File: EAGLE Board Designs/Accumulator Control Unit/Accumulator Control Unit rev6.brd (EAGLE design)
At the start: 255 x 73 mm, 302 parts, among them J1 CONNECTOR-12_MF_T_V_, J2 CONNECTOR-6_μF_T_V_BLACK, J3 CONNECTOR-4_μF_T_V_BLACK, J4 CONNECTOR-2_MF_T_V_, J5 CONNECTOR-8_μF_T_V_BLACK, J6 CONNECTOR-16_MF_T_V_, J9 CONNECTOR-2_MF_T_V_, Q1 TRANSISTOR_N_MOS__PMV15ENEA, Q2 TRANSISTOR_N_MOS__PMV15ENEA, Q3 TRANSISTOR_N_MOS__PMV15ENEA, Q4 TRANSISTOR_N_MOS__PMV15ENEA, Q5 TRANSISTOR_P_MOS_SOT-23_DMP30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, T1 TRANSFORMER_HM2112ZNLT_AIRGAP, U1 VOLTAGE_REGULATOR_SOT-223_3.3V, U10 TCAN1051HQV-Q1, U11 OPAMP_1_CHANNEL_OPA991, U12 OPAMP_1_CHANNEL_OPA991, U13 OPAMP_1_CHANNEL_OPA991, U14 RELAY_SOLIDSTATE_NO_DIP-4, U15 LM555, U16 OPAMP_1_CHANNEL_OPA991, U17 OPAMP_2_CHANNEL_OPA_2991, U18 OPAMP_1_CHANNEL_OPA991, U19 OPAMP_2_CHANNEL_OPA_2991, U2 RELAY_SOLIDSTATE_NO_DIP-4, U20 LOGICGATE_BUFFER, U21 ADM8316WBX30, U22 OPAMP_1_CHANNEL_OPA991, U23 LOGICGATE_AND_DCK3, U24 LOGICGATE_AND_DCK3, U25 LOGICGATE_AND_DCK3, U26 OPAMP_1_CHANNEL_OPA991, U27 ADG1423, U28 OPAMP_1_CHANNEL_OPA991, U29 OPAMP_2_CHANNEL_OPA_2991, U3 RELAY_SOLIDSTATE_NO_DIP-4, U30 OPAMP_1_CHANNEL_OPA991, U31 OPAMP_2_CHANNEL_OPA_2991, U32 LTC6820, U33 OPAMP_1_CHANNEL_OPA991, U4 OPAMP_1_CHANNEL_OPA991, U5 OPAMP_1_CHANNEL_OPA991, U6 TCAN1051HQV-Q1, U7 LTC6820, U8 OPAMP_1_CHANNEL_OPA991, U9 OPAMP_1_CHANNEL_OPA991

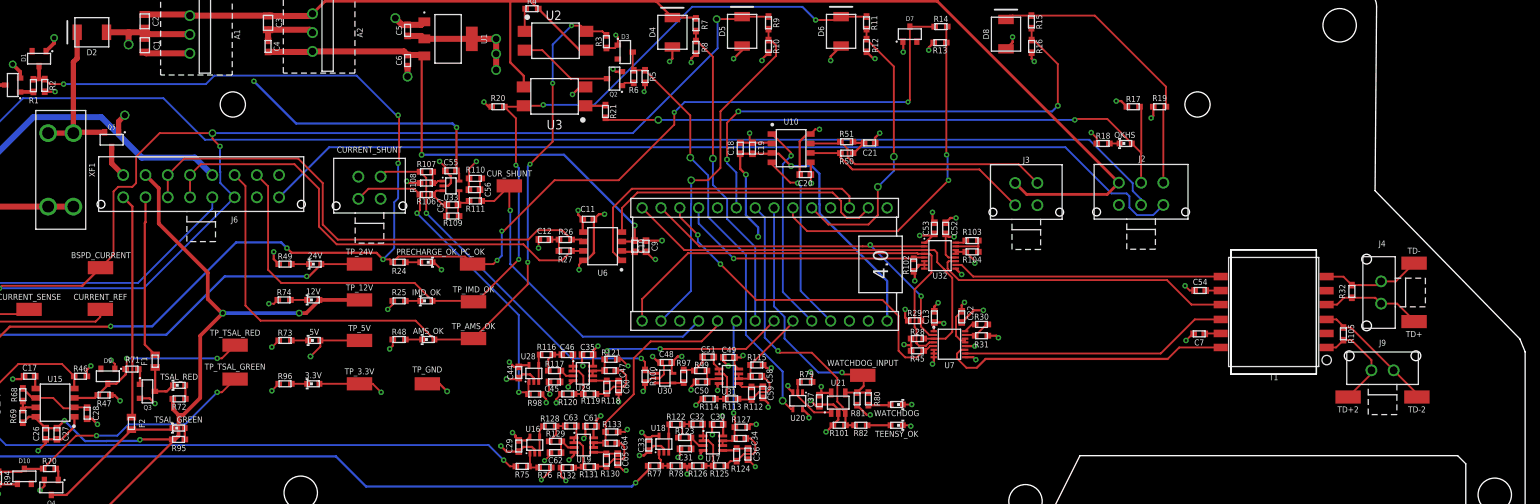
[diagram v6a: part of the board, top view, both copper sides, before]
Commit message: Added HV silkscreen
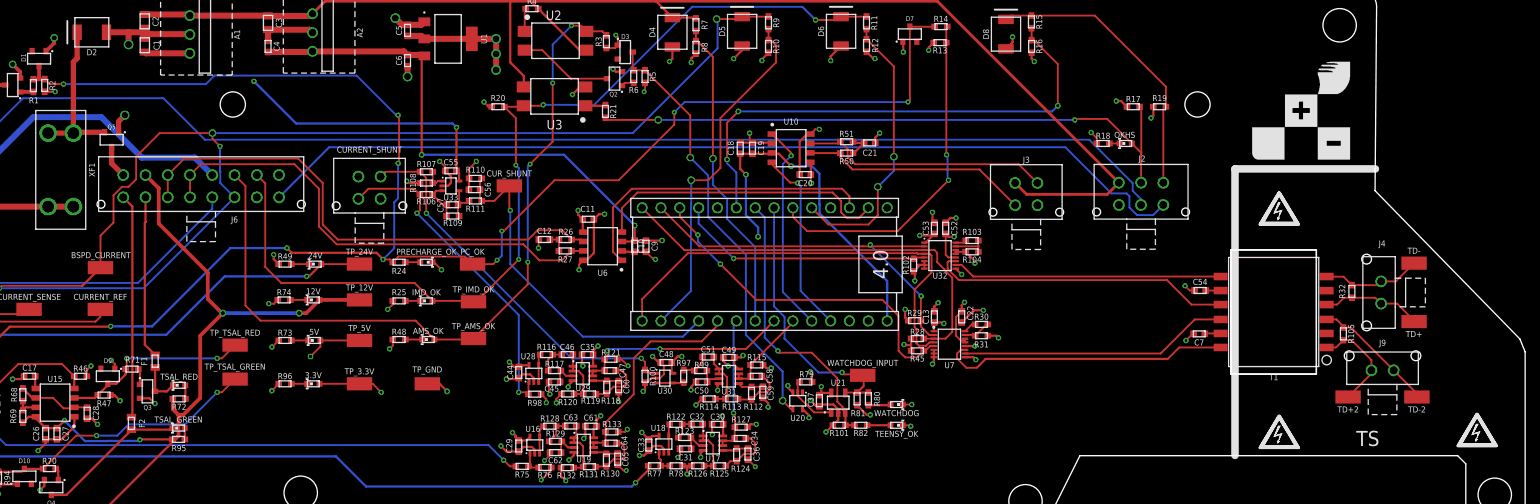
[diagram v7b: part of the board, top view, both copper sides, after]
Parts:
- added U$10, U$11, U$13, U$14, U$15, U$16: (no value), HyTechManufacturing:HV_MEDIUM
- added U$12: (no value), HyTechManufacturing:LOGO_HYTECH_SQUARE_EXTRA_LARGE
- added U$9: (no value), HyTechManufacturing:TS
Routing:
- net PRECHARGE_OK: track 263.4 -> 262.7 mm
- net BSPD_CURRENT: track 179.6 -> 179.0 mm
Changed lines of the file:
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@@
 <wire x1="249.428" y1="0" x2="252.5" y2="0" width="0" layer="20"/>
 <wire x1="252.5" y1="0" x2="255" y2="2.5" width="0" layer="20"/>
+<wire x1="215.9" y1="10.033" x2="215.9" y2="48.641" width="1.016" layer="21"/>
+<wire x1="215.9" y1="48.641" x2="234.823" y2="48.641" width="1.016" layer="21"/>
+<wire x1="234.823" y1="48.387" x2="234.569" y2="48.641" width="1.016" layer="22"/>
+<wire x1="234.569" y1="48.641" x2="215.9" y2="48.641" width="1.016" layer="22"/>
+<wire x1="215.9" y1="48.641" x2="215.773" y2="10.287" width="1.016" layer="22"/>
+<wire x1="215.773" y1="10.287" x2="215.9" y2="10.16" width="1.016" layer="22"/>
 </plain>
 <attributes>
@@
 <attribute name="NAME" x="64.516" y="54.61" size="0.635" layer="25" font="vector" align="top-center"/>
 </element>
+<element name="U$10" library="HyTechManufacturing" package="HV_MEDIUM" value="" x="221.869" y="13.208" smashed="yes"/>
+<element name="U$11" library="HyTechManufacturing" package="HV_MEDIUM" value="" x="248.539" y="13.462" smashed="yes"/>
+<element name="U$12" library="HyTechManufacturing" package="LOGO_HYTECH_SQUARE_EXTRA_LARGE" value="" x="224.79" y="56.515" smashed="yes"/>
+<element name="U$9" library="HyTechManufacturing" package="TS" value="" x="233.807" y="12.319" smashed="yes"/>
+<element name="U$13" library="HyTechManufacturing" package="HV_MEDIUM" value="" x="221.869" y="43.307" smashed="yes"/>
+<element name="U$14" library="HyTechManufacturing" package="HV_MEDIUM" value="" x="248.539" y="13.462" smashed="yes"/>
+<element name="U$15" library="HyTechManufacturing" package="HV_MEDIUM" value="" x="221.869" y="13.208" smashed="yes"/>
+<element name="U$16" library="HyTechManufacturing" package="HV_MEDIUM" value="" x="221.869" y="43.307" smashed="yes"/>
 </elements>
 <signals>
@@
 <via x="204.597" y="55.499" extent="1-16" drill="0.35"/>
 <wire x1="87.034" y1="35.814" x2="86.36" y2="36.488" width="0.3048" layer="1"/>
-<wire x1="86.36" y1="36.488" x2="86.36" y2="37.465" width="0.3048" layer="1"/>
-<via x="86.36" y="37.465" extent="1-16" drill="0.35"/>
+<wire x1="86.36" y1="36.488" x2="86.36" y2="37.084" width="0.3048" layer="1"/>
+<via x="86.36" y="37.084" extent="1-16" drill="0.35"/>
 <wire x1="133.2865" y1="61.7474" x2="132.4356" y2="61.7474" width="0.3048" layer="1"/>
 <wire x1="132.4356" y1="61.7474" x2="132.08" y2="62.103" width="0.3048" layer="1"/>
@@
 <wire x1="42.164" y1="8.1414" x2="43.7909" y2="8.1414" width="0.3048" layer="1"/>
 <wire x1="43.7909" y1="8.1414" x2="43.815" y2="8.1655" width="0.3048" layer="1"/>
-<wire x1="55.626" y1="13.9065" x2="55.626" y2="13.704" width="0.3048" layer="1"/>
 <wire x1="57.15" y1="13.704" x2="55.626" y2="13.704" width="0.3048" layer="1"/>
 <wire x1="110.986" y1="48.387" x2="111.336" y2="48.037" width="0.3048" layer="1"/>
@@
 <wire x1="52.5526" y1="14.4408" x2="53.3518" y2="15.24" width="0.3048" layer="1"/>
 <wire x1="53.3518" y1="15.24" x2="54.2925" y2="15.24" width="0.3048" layer="1"/>
-<wire x1="55.626" y1="13.704" x2="54.2925" y2="15.0375" width="0.3048" layer="1"/>
 <wire x1="54.2925" y1="15.0375" x2="54.2925" y2="15.24" width="0.3048" layer="1"/>
+<wire x1="55.626" y1="13.704" x2="54.2925" y2="15.0375" width="0.3048" layer="1"/>
 </signal>
 <signal name="BSPD_CURRENT">
@@
 <wire x1="78.105" y1="52.705" x2="78.105" y2="53.467" width="0.254" layer="1"/>
 <wire x1="67.818" y1="50.292" x2="70.993" y2="53.467" width="0.254" layer="1"/>
-<wire x1="64.77" y1="37.084" x2="64.77" y2="45.593" width="0.254" layer="1"/>
-<wire x1="64.77" y1="45.593" x2="65.405" y2="46.228" width="0.254" layer="1"/>
-<wire x1="65.405" y1="46.228" x2="67.31" y2="46.228" width="0.254" layer="1"/>
-<wire x1="67.31" y1="46.228" x2="67.818" y2="46.736" width="0.254" layer="1"/>
-<wire x1="63.0174" y1="35.3314" x2="64.77" y2="37.084" width="0.254" layer="1"/>
-<wire x1="67.818" y1="46.736" x2="67.818" y2="50.292" width="0.254" layer="1"/>
+<wire x1="64.77" y1="41.402" x2="64.77" y2="45.085" width="0.254" layer="1"/>
+<wire x1="64.77" y1="45.085" x2="65.913" y2="46.228" width="0.254" layer="1"/>
+<wire x1="65.913" y1="46.228" x2="66.802" y2="46.228" width="0.254" layer="1"/>
+<wire x1="66.802" y1="46.228" x2="67.818" y2="47.244" width="0.254" layer="1"/>
+<wire x1="64.77" y1="41.402" x2="63.0174" y2="39.6494" width="0.254" layer="1"/>
+<wire x1="63.0174" y1="35.3314" x2="63.0174" y2="39.6494" width="0.254" layer="1"/>
+<wire x1="67.818" y1="47.244" x2="67.818" y2="50.292" width="0.254" layer="1"/>
 </signal>
 <signal name="IMD_OK">
@@
 <contactref element="R11" pad="1"/>
 <contactref element="D6" pad="2"/>
-<wire x1="84.083" y1="47.817" x2="85.598" y2="46.302" width="0.254" layer="1"/>
+<wire x1="84.083" y1="47.817" x2="85.217" y2="46.683" width="0.254" layer="1"/>
 <wire x1="105.346" y1="33.274" x2="107.759" y2="30.861" width="0.254" layer="1"/>
-<wire x1="85.598" y1="46.302" x2="85.598" y2="35.052" width="0.254" layer="1"/>
-<wire x1="85.598" y1="35.052" x2="87.376" y2="33.274" width="0.254" layer="1"/>
+<wire x1="85.217" y1="46.683" x2="85.217" y2="35.433" width="0.254" layer="1"/>
+<wire x1="85.217" y1="35.433" x2="87.376" y2="33.274" width="0.254" layer="1"/>
 <wire x1="87.376" y1="33.274" x2="105.346" y2="33.274" width="0.254" layer="1"/>
 <wire x1="162.814" y1="69.163" x2="163.068" y2="69.163" width="0.254" layer="1"/>
@@
 <wire x1="64.3382" y1="27.3812" x2="50.7902" y2="27.3812" width="0.3048" layer="1"/>
 <wire x1="64.389" y1="27.432" x2="69.977" y2="27.432" width="0.3048" layer="16"/>
-<wire x1="69.977" y1="27.432" x2="81.28" y2="38.735" width="0.3048" layer="16"/>
-<wire x1="81.28" y1="38.735" x2="87.376" y2="38.735" width="0.3048" layer="16"/>
-<wire x1="87.376" y1="38.735" x2="88.138" y2="37.973" width="0.3048" layer="16"/>
+<wire x1="69.977" y1="27.432" x2="80.518" y2="37.973" width="0.3048" layer="16"/>
+<wire x1="80.518" y1="37.973" x2="88.138" y2="37.973" width="0.3048" layer="16"/>
 <via x="88.138" y="37.973" extent="1-16" drill="0.35"/>
 <wire x1="100.203" y1="37.338" x2="88.773" y2="37.338" width="0.3048" layer="1"/>
@@
 <wire x1="142.621" y1="47.117" x2="144.907" y2="47.117" width="0.254" layer="1"/>
 <wire x1="146.558" y1="48.768" x2="144.907" y2="47.117" width="0.254" layer="1"/>
-<wire x1="146.558" y1="56.388" x2="154.051" y2="63.881" width="0.254" layer="1"/>
-<wire x1="154.051" y1="63.881" x2="154.051" y2="65.278" width="0.254" layer="1"/>
+<wire x1="146.558" y1="55.499" x2="154.051" y2="62.992" width="0.254" layer="1"/>
+<wire x1="154.051" y1="62.992" x2="154.051" y2="65.278" width="0.254" layer="1"/>
 <wire x1="154.051" y1="65.278" x2="153.035" y2="66.294" width="0.254" layer="1"/>
-<wire x1="146.558" y1="48.768" x2="146.558" y2="56.388" width="0.254" layer="1"/>
+<wire x1="146.558" y1="48.768" x2="146.558" y2="55.499" width="0.254" layer="1"/>
 <contactref element="A3" pad="D14"/>
 </signal>

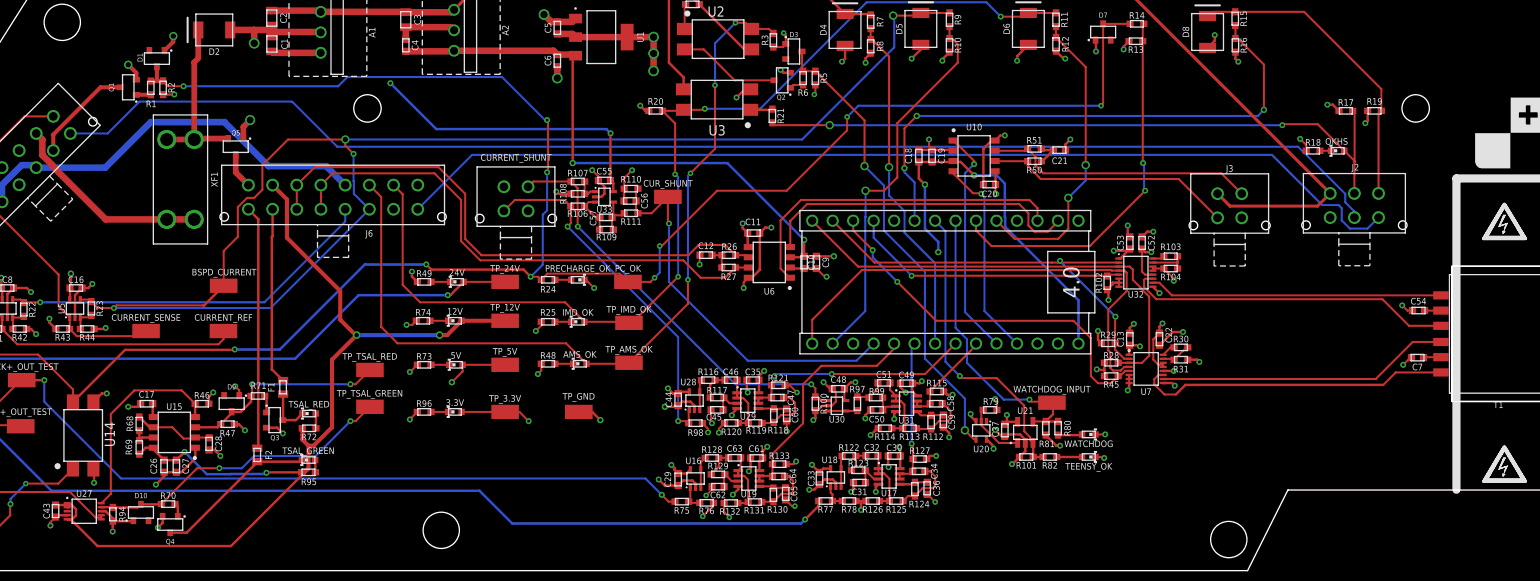
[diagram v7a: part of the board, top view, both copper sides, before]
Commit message: added Silkscreen stuff
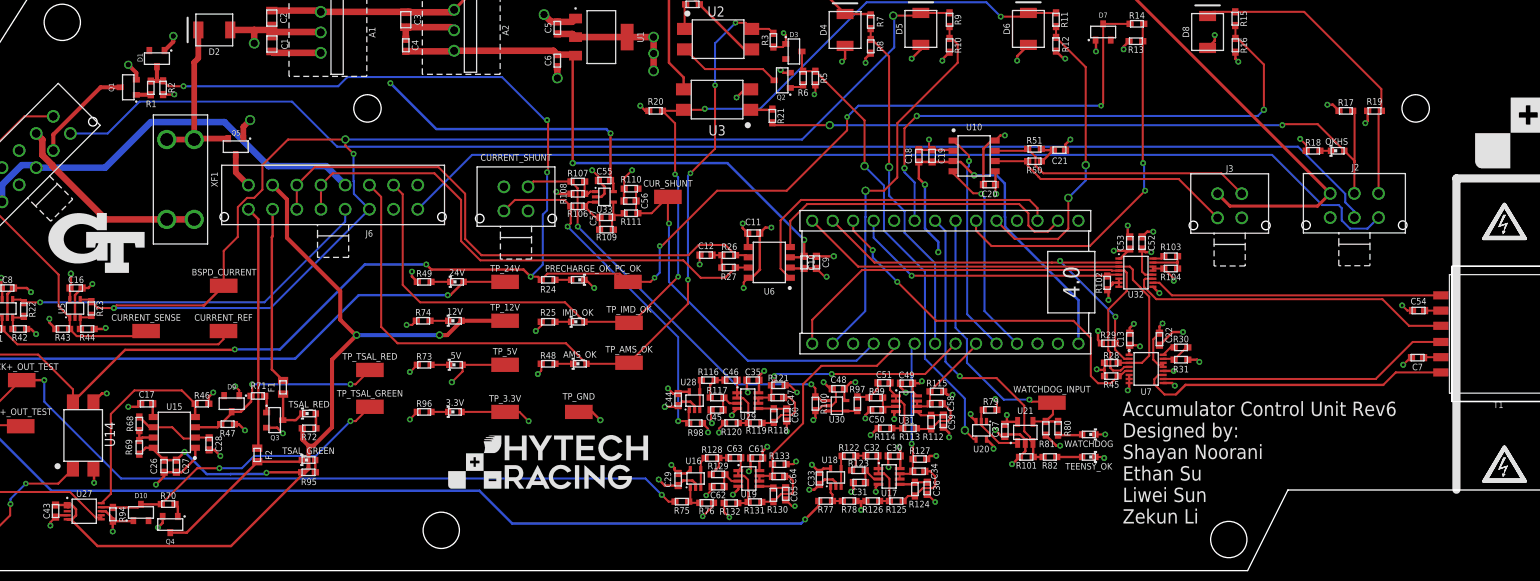
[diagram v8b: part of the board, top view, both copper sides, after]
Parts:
- added U$17: (no value), HyTechManufacturing:LOGO_GT_MEDIUM
- added U$18: (no value), HyTechManufacturing:LOGO_HYTECH_MEDIUM
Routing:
- net EM_CTX: track 28.4 -> 27.6 mm
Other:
- board text added: "Accumulator Control Unit Rev6 Designed by: Shayan Noorani Ethan Su Liwei Sun Zekun Li"
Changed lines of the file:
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@@
 <wire x1="215.9" y1="48.641" x2="215.773" y2="10.287" width="1.016" layer="22"/>
 <wire x1="215.773" y1="10.287" x2="215.9" y2="10.16" width="1.016" layer="22"/>
+<text x="174.498" y="5.842" size="1.778" layer="21" font="vector">Accumulator Control Unit Rev6
+Designed by:
+Shayan Noorani
+Ethan Su
+Liwei Sun
+Zekun Li</text>
 </plain>
 <attributes>
@@
 <element name="U$15" library="HyTechManufacturing" package="HV_MEDIUM" value="" x="221.869" y="13.208" smashed="yes"/>
 <element name="U$16" library="HyTechManufacturing" package="HV_MEDIUM" value="" x="221.869" y="43.307" smashed="yes"/>
+<element name="U$17" library="HyTechManufacturing" package="LOGO_GT_MEDIUM" value="" x="47.244" y="40.64" smashed="yes"/>
+<element name="U$18" library="HyTechManufacturing" package="LOGO_HYTECH_MEDIUM" value="" x="90.805" y="10.16" smashed="yes"/>
 </elements>
 <signals>
@@
 <contactref element="U32" pad="12"/>
 <polygon width="0" layer="15" rank="2">
-<vertex x="-7.239" y="86.868"/>
-<vertex x="-7.239" y="-3.175"/>
+<vertex x="-9.017" y="81.788"/>
+<vertex x="-9.017" y="-1.397"/>
 <vertex x="-1.778" y="-8.636"/>
 <vertex x="199.937915625" y="-8.636"/>
 <vertex x="210.947" y="2.373084375"/>
 <vertex x="210.947" y="81.915"/>
-<vertex x="-2.286" y="81.915"/>
+<vertex x="-9.144" y="81.915"/>
 </polygon>
 <contactref element="U31" pad="8"/>
@@
 <contactref element="U2" pad="2"/>
 <contactref element="Q2" pad="3"/>
-<wire x1="120.183" y1="64.643" x2="122.555" y2="64.643" width="0.254" layer="1"/>
-<wire x1="126.3904" y1="60.8076" x2="131.2799" y2="60.8076" width="0.254" layer="1"/>
-<wire x1="122.555" y1="64.643" x2="126.3904" y2="60.8076" width="0.254" layer="1"/>
+<wire x1="120.183" y1="64.643" x2="120.269" y2="64.643" width="0.254" layer="1"/>
+<wire x1="129.8829" y1="62.2046" x2="122.7074" y2="62.2046" width="0.254" layer="1"/>
+<wire x1="129.8829" y1="62.2046" x2="131.2799" y2="60.8076" width="0.254" layer="1"/>
+<wire x1="120.269" y1="64.643" x2="122.7074" y2="62.2046" width="0.254" layer="1"/>
 </signal>
 <signal name="N$30">
 <contactref element="R6" pad="2"/>
 <contactref element="Q2" pad="1"/>
-<wire x1="133.2865" y1="59.8678" x2="133.6557" y2="60.237" width="0.254" layer="1"/>
-<wire x1="133.6557" y1="60.237" x2="134.874" y2="60.237" width="0.254" layer="1"/>
+<wire x1="133.2865" y1="59.8678" x2="133.4017" y2="59.983" width="0.254" layer="1"/>
+<wire x1="134.62" y1="59.983" x2="134.874" y2="60.237" width="0.254" layer="1"/>
+<wire x1="134.62" y1="59.983" x2="133.4017" y2="59.983" width="0.254" layer="1"/>
 </signal>
 <signal name="AMS_OK_3.3V">
@@
 <signal name="EM_CTX">
 <contactref element="U10" pad="1"/>
-<via x="156.083" y="50.419" extent="1-16" drill="0.35"/>
+<via x="155.448" y="50.8" extent="1-16" drill="0.35"/>
 <wire x1="153.4795" y1="53.34" x2="154.0891" y2="52.7304" width="0.254" layer="1"/>
 <wire x1="154.0891" y1="52.7304" x2="154.16673125" y2="52.7304" width="0.254" layer="1"/>
-<wire x1="154.16673125" y1="52.7304" x2="156.083" y2="50.81413125" width="0.254" layer="1"/>
-<wire x1="156.083" y1="50.81413125" x2="156.083" y2="50.419" width="0.254" layer="1"/>
-<wire x1="156.083" y1="50.419" x2="154.9654" y2="49.3014" width="0.254" layer="16"/>
-<wire x1="154.9654" y1="49.3014" x2="154.9654" y2="32.0546" width="0.254" layer="16"/>
-<wire x1="154.9654" y1="32.0546" x2="158.864" y2="28.156" width="0.254" layer="16"/>
+<wire x1="154.16673125" y1="52.7304" x2="155.448" y2="51.44913125" width="0.254" layer="1"/>
+<wire x1="155.448" y1="51.44913125" x2="155.448" y2="50.8" width="0.254" layer="1"/>
+<wire x1="155.448" y1="50.8" x2="155.448" y2="50.165" width="0.254" layer="16"/>
+<wire x1="155.448" y1="50.165" x2="155.2194" y2="49.9364" width="0.254" layer="16"/>
+<wire x1="155.2194" y1="49.9364" x2="155.2194" y2="31.8006" width="0.254" layer="16"/>
+<wire x1="155.2194" y1="31.8006" x2="158.864" y2="28.156" width="0.254" layer="16"/>
 <contactref element="A3" pad="D22"/>
 </signal>
@@
 </board>
 </drawing>
+<compatibility>
+<note version="6.3" minversion="6.2.2" severity="warning">
+Since Version 6.2.2 text objects can contain more than one line,
+which will not be processed correctly with this version.
+</note>
+</compatibility>
 </eagle>
